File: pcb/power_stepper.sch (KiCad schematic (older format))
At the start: 48 parts, among them J2 Screw_Terminal, U16 UCC12040, U17 ISO7762, U2 powerSTEP01

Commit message: relayout
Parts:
- C1: footprint Capacitor_SMD:C_1206_3216Metric -> Capacitor_SMD:C_0805_2012Metric
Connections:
- net SENSEA_P: now reaches JP1.1 (A), RS1.2, RS2.2, RS3.2, RS7.2, U2.20 (SENSEA_S), U2.34 (SENSEA_P), U2.35 (SENSEA_P), U2.36 (SENSEA_P), U2.39 (SENSEA_P), U2.40 (SENSEA_P), U2.41 (SENSEA_P), U2.E10 (SENSEA_P), U2.E11 (SENSEA_P)
- net SENSEB_P: now reaches JP2.1 (A), RS4.2, RS5.2, RS6.2, RS8.2, U2.77 (SENSEB_P), U2.78 (SENSEB_P), U2.79 (SENSEB_P), U2.82 (SENSEB_P), U2.83 (SENSEB_P), U2.84 (SENSEB_P), U2.9 (SENSEB_S), U2.E12 (SENSEB_P), U2.E13 (SENSEB_P)
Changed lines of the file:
@@
 F 0 "C1" H 3618 7246 50  0000 L CNN
 F 1 "22uF" H 3618 7155 50  0000 L CNN
-F 2 "Capacitor_SMD:C_1206_3216Metric" H 3538 7050 50  0001 C CNN
+F 2 "Capacitor_SMD:C_0805_2012Metric" H 3538 7050 50  0001 C CNN
 F 3 "~" H 3500 7200 50  0001 C CNN
 	1    3500 7200
@@
 Text Label 3100 3050 2    50   ~ 0
 SM_SI
+Text Label 7550 4100 0    39   ~ 0
+SENSEB_P
+Text Label 7550 2850 0    39   ~ 0
+SENSEA_P
 $EndSCHEMATC

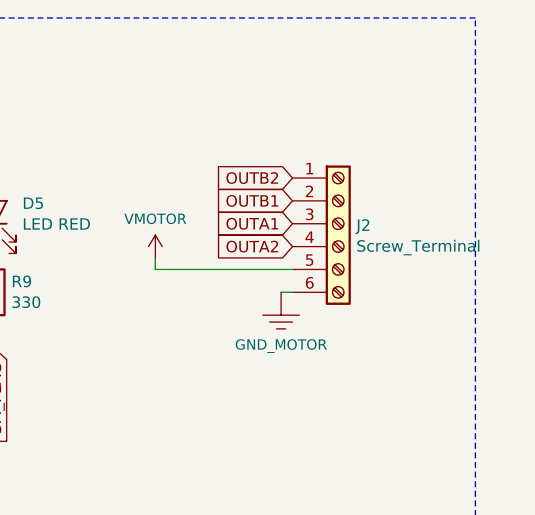
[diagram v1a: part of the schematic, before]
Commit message: stepper motor connector changed
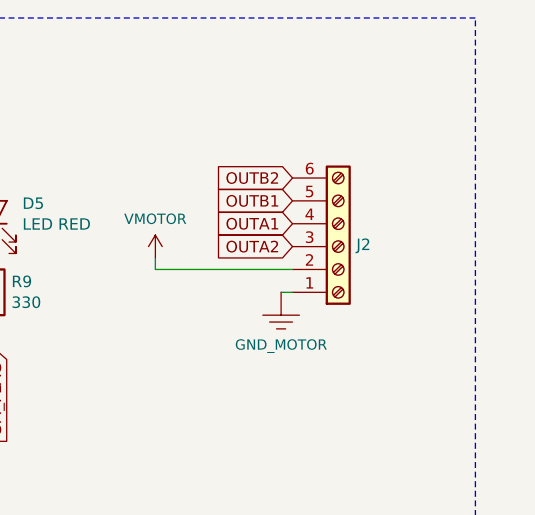
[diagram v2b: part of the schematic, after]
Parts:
- J2: value Screw_Terminal -> 1757284; footprint TerminalBlock_Phoenix:TerminalBlock_Phoenix_PT-1,5-6-5.0-H_1x06_P5.00mm_Horizontal -> Connector_Phoenix_MSTB:PhoenixContact_MSTBA_2,5_6-G-5,08_1x06_P5.08mm_Horizontal; DigiKey (none) -> 1757284
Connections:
- net GND_MOTOR: now also J2.1 (Pin_1); no longer J2.6 (Pin_6)
- net OUTA1: now also J2.4 (Pin_4); no longer J2.3 (Pin_3)
- net OUTA2: now also J2.3 (Pin_3); no longer J2.4 (Pin_4)
- net OUTB1: now also J2.5 (Pin_5); no longer J2.2 (Pin_2)
- net OUTB2: now also J2.6 (Pin_6); no longer J2.1 (Pin_1)
- net VMOTOR: now also J2.2 (Pin_2); no longer J2.5 (Pin_5)
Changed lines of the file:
@@
 EESchema Schematic File Version 4
+LIBS:keep_breathing_ctrl-cache
 EELAYER 30 0
 EELAYER END
@@
 L Connector:Screw_Terminal_01x06 J2
 U 1 1 5C39C166
-P 10500 1400
-F 0 "J2" H 10579 1392 50  0000 L CNN
-F 1 "Screw_Terminal" H 10579 1301 50  0000 L CNN
-F 2 "TerminalBlock_Phoenix:TerminalBlock_Phoenix_PT-1,5-6-5.0-H_1x06_P5.00mm_Horizontal" H 10500 1400 50  0001 C CNN
-F 3 "~" H 10500 1400 50  0001 C CNN
-	1    10500 1400
-	1    0    0    -1
-$EndComp
-$Comp
+P 10500 1500
+F 0 "J2" H 10579 1492 50  0000 L CNN
+F 1 "1757284" H 10579 1401 50  0001 L CNN
+F 2 "Connector_Phoenix_MSTB:PhoenixContact_MSTBA_2,5_6-G-5,08_1x06_P5.08mm_Horizontal" H 10500 1500 50  0001 C CNN
+F 3 "~" H 10500 1500 50  0001 C CNN
+F 4 "1757284" H 10500 1500 50  0001 C CNN "DigiKey"
+	1    10500 1500
+	1    0    0    1
+$EndComp
+$Comp

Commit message: routing isolators
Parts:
- D3, D5: footprint Diode_SMD:D_0805_2012Metric -> Diode_SMD:D_0603_1608Metric
- R11: footprint Resistor_SMD:R_0603_1608Metric -> Resistor_SMD:R_0402_1005Metric
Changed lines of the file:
@@
 F 0 "D5" V 9038 1232 50  0000 R CNN
 F 1 "LED RED" V 8947 1232 50  0000 R CNN
-F 2 "Diode_SMD:D_0805_2012Metric" H 9000 1350 50  0001 C CNN
+F 2 "Diode_SMD:D_0603_1608Metric" H 9000 1350 50  0001 C CNN
 F 3 "~" H 9000 1350 50  0001 C CNN
 	1    9000 1350
@@
 Wire Wire Line
 	9000 1550 9000 1500
-$Comp
-L Device:R R11
-U 1 1 5BEF92F7
-P 8900 4800
-F 0 "R11" H 8970 4846 50  0000 L CNN
-F 1 "330" H 8970 4755 50  0000 L CNN
-F 2 "Resistor_SMD:R_0603_1608Metric" V 8830 4800 50  0001 C CNN
-F 3 "~" H 8900 4800 50  0001 C CNN
-	1    8900 4800
-	1    0    0    -1
-$EndComp
-$Comp
-L Device:LED D3
-U 1 1 5BEF93CE
-P 8900 4450
-F 0 "D3" V 8938 4333 50  0000 R CNN
-F 1 "LED GRN" V 8847 4333 50  0000 R CNN
-F 2 "Diode_SMD:D_0805_2012Metric" H 8900 4450 50  0001 C CNN
-F 3 "~" H 8900 4450 50  0001 C CNN
-	1    8900 4450
-	0    -1   -1   0
-$EndComp
-Wire Wire Line
-	8900 4600 8900 4650
-Wire Wire Line
-	8900 4300 8900 4200
-Wire Wire Line
-	8900 4950 8900 5050
 Wire Wire Line
 	6650 2950 6650 2850
@@
 Wire Wire Line
 	3150 7000 3500 7000
-$Comp
-L ventilator-PowerSymbols:3V3_M #SUPPLY0106
-U 1 1 5EB9B2A5
-P 8900 4200
-F 0 "#SUPPLY0106" H 8950 4200 45  0001 L BNN
-F 1 "3V3_M" H 8900 4370 45  0000 C CNN
-F 2 "" H 8900 4200 50  0001 C CNN
-F 3 "" H 8900 4200 60  0001 C CNN
-	1    8900 4200
-	1    0    0    -1
-$EndComp
 $Comp
 L ventilator-PowerSymbols:3V3_M #SUPPLY0107
@@
 $EndComp
 $Comp
+L ventilator-PowerSymbols:GND_MOTOR #GND0109
+U 1 1 5EB3C9E7
+P 10150 5200
+F 0 "#GND0109" H 10200 5150 45  0001 L BNN
+F 1 "GND_MOTOR" H 10150 4970 45  0000 C CNN
+F 2 "" H 10150 5200 50  0001 C CNN
+F 3 "" H 10150 5100 60  0001 C CNN
+	1    10150 5200
+	1    0    0    -1
+$EndComp
+$Comp
+L ventilator-PowerSymbols:GND_MOTOR #GND0110
+U 1 1 5EB42E98
+P 4150 7450
+F 0 "#GND0110" H 4200 7400 45  0001 L BNN
+F 1 "GND_MOTOR" H 4150 7220 45  0000 C CNN
+F 2 "" H 4150 7450 50  0001 C CNN
+F 3 "" H 4150 7350 60  0001 C CNN
+	1    4150 7450
+	1    0    0    -1
+$EndComp
+$Comp
+L ventilator-PowerSymbols:GND_MOTOR #GND0111
+U 1 1 5EB70716
+P 3650 6600
+F 0 "#GND0111" H 3700 6550 45  0001 L BNN
+F 1 "GND_MOTOR" H 3650 6370 45  0000 C CNN
+F 2 "" H 3650 6600 50  0001 C CNN
+F 3 "" H 3650 6500 60  0001 C CNN
+	1    3650 6600
+	1    0    0    -1
+$EndComp
+$Comp
+L ventilator-PowerSymbols:GND_MOTOR #GND0112
+U 1 1 5EB70F8C
+P 2800 4000
+F 0 "#GND0112" H 2850 3950 45  0001 L BNN
+F 1 "GND_MOTOR" H 2800 3770 45  0000 C CNN
+F 2 "" H 2800 4000 50  0001 C CNN
+F 3 "" H 2800 3900 60  0001 C CNN
+	1    2800 4000
+	1    0    0    -1
+$EndComp
+$Comp
+L ventilator-PowerSymbols:GND_MOTOR #GND0114
+U 1 1 5EB73041
+P 3550 2900
+F 0 "#GND0114" H 3600 2850 45  0001 L BNN
+F 1 "GND_MOTOR" H 3550 2670 45  0000 C CNN
+F 2 "" H 3550 2900 50  0001 C CNN
+F 3 "" H 3550 2800 60  0001 C CNN
+	1    3550 2900
+	1    0    0    -1
+$EndComp
+$Comp
+L ventilator-PowerSymbols:GND_MOTOR #GND0115
+U 1 1 5EBD4224
+P 6500 6950
+F 0 "#GND0115" H 6550 6900 45  0001 L BNN
+F 1 "GND_MOTOR" H 6500 6720 45  0000 C CNN
+F 2 "" H 6500 6950 50  0001 C CNN
+F 3 "" H 6500 6850 60  0001 C CNN
+	1    6500 6950
+	1    0    0    -1
+$EndComp
+Wire Wire Line
+	2700 3200 3100 3200
+Wire Wire Line
+	2700 3050 3100 3050
+Text Label 3100 3050 2    50   ~ 0
+SM_SI
+Text Label 7550 4100 0    39   ~ 0
+SENSEB_P
+Text Label 7550 2850 0    39   ~ 0
+SENSEA_P
+$Comp
 L ventilator-PowerSymbols:GND_MOTOR #GND0108
 U 1 1 5EAD8892
@@
 $EndComp
 $Comp
-L ventilator-PowerSymbols:GND_MOTOR #GND0109
-U 1 1 5EB3C9E7
-P 10150 5200
-F 0 "#GND0109" H 10200 5150 45  0001 L BNN
-F 1 "GND_MOTOR" H 10150 4970 45  0000 C CNN
-F 2 "" H 10150 5200 50  0001 C CNN
-F 3 "" H 10150 5100 60  0001 C CNN
-	1    10150 5200
-	1    0    0    -1
-$EndComp
-$Comp
-L ventilator-PowerSymbols:GND_MOTOR #GND0110
-U 1 1 5EB42E98
-P 4150 7450
-F 0 "#GND0110" H 4200 7400 45  0001 L BNN
-F 1 "GND_MOTOR" H 4150 7220 45  0000 C CNN
-F 2 "" H 4150 7450 50  0001 C CNN
-F 3 "" H 4150 7350 60  0001 C CNN
-	1    4150 7450
-	1    0    0    -1
-$EndComp
-$Comp
-L ventilator-PowerSymbols:GND_MOTOR #GND0111
-U 1 1 5EB70716
-P 3650 6600
-F 0 "#GND0111" H 3700 6550 45  0001 L BNN
-F 1 "GND_MOTOR" H 3650 6370 45  0000 C CNN
-F 2 "" H 3650 6600 50  0001 C CNN
-F 3 "" H 3650 6500 60  0001 C CNN
-	1    3650 6600
-	1    0    0    -1
-$EndComp
-$Comp
-L ventilator-PowerSymbols:GND_MOTOR #GND0112
-U 1 1 5EB70F8C
-P 2800 4000
-F 0 "#GND0112" H 2850 3950 45  0001 L BNN
-F 1 "GND_MOTOR" H 2800 3770 45  0000 C CNN
-F 2 "" H 2800 4000 50  0001 C CNN
-F 3 "" H 2800 3900 60  0001 C CNN
-	1    2800 4000
-	1    0    0    -1
-$EndComp
-$Comp
-L ventilator-PowerSymbols:GND_MOTOR #GND0114
-U 1 1 5EB73041
-P 3550 2900
-F 0 "#GND0114" H 3600 2850 45  0001 L BNN
-F 1 "GND_MOTOR" H 3550 2670 45  0000 C CNN
-F 2 "" H 3550 2900 50  0001 C CNN
-F 3 "" H 3550 2800 60  0001 C CNN
-	1    3550 2900
-	1    0    0    -1
-$EndComp
-$Comp
-L ventilator-PowerSymbols:GND_MOTOR #GND0115
-U 1 1 5EBD4224
-P 6500 6950
-F 0 "#GND0115" H 6550 6900 45  0001 L BNN
-F 1 "GND_MOTOR" H 6500 6720 45  0000 C CNN
-F 2 "" H 6500 6950 50  0001 C CNN
-F 3 "" H 6500 6850 60  0001 C CNN
-	1    6500 6950
-	1    0    0    -1
-$EndComp
-Wire Wire Line
-	2700 3200 3100 3200
-Wire Wire Line
-	2700 3050 3100 3050
-Text Label 3100 3050 2    50   ~ 0
-SM_SI
-Text Label 7550 4100 0    39   ~ 0
-SENSEB_P
-Text Label 7550 2850 0    39   ~ 0
-SENSEA_P
+L ventilator-PowerSymbols:3V3_M #SUPPLY0106
+U 1 1 5EB9B2A5
+P 8900 4200
+F 0 "#SUPPLY0106" H 8950 4200 45  0001 L BNN
+F 1 "3V3_M" H 8900 4370 45  0000 C CNN
+F 2 "" H 8900 4200 50  0001 C CNN
+F 3 "" H 8900 4200 60  0001 C CNN
+	1    8900 4200
+	1    0    0    -1
+$EndComp
+Wire Wire Line
+	8900 4950 8900 5050
+Wire Wire Line
+	8900 4300 8900 4200
+Wire Wire Line
+	8900 4600 8900 4650
+$Comp
+L Device:LED D3
+U 1 1 5BEF93CE
+P 8900 4450
+F 0 "D3" V 8938 4333 50  0000 R CNN
+F 1 "LED GRN" V 8847 4333 50  0000 R CNN
+F 2 "Diode_SMD:D_0603_1608Metric" H 8900 4450 50  0001 C CNN
+F 3 "~" H 8900 4450 50  0001 C CNN
+	1    8900 4450
+	0    -1   -1   0
+$EndComp
+$Comp
+L Device:R R11
+U 1 1 5BEF92F7
+P 8900 4800
+F 0 "R11" H 8970 4846 50  0000 L CNN
+F 1 "330" H 8970 4755 50  0000 L CNN
+F 2 "Resistor_SMD:R_0402_1005Metric" V 8830 4800 50  0001 C CNN
+F 3 "~" H 8900 4800 50  0001 C CNN
+	1    8900 4800
+	1    0    0    -1
+$EndComp
 $EndSCHEMATC

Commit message: updating planes
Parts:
- added C74: 0.1uF, Capacitor_SMD:C_0402_1005Metric, symbol Device:C_Small
- R39: value SEL -> 100k
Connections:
- net GND: now also U16.4 (SYNC), C74.2
- net +5V: now reaches C33.1, C34.1, U16.1 (EN), U16.3 (VINP)
- net +3V3: now reaches U17.1 (VCC1)
- net +3V3: now also C74.1
- no-connect marks 3 -> 4
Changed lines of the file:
@@
 U 1 1 5E9880D0
 P 2100 1550
+AR Path="/5E9880D0" Ref="U16"  Part="1"
+AR Path="/5E968E64/5E9880D0" Ref="U16"  Part="1"
 F 0 "U16" H 1650 2250 50  0000 L CNB
 F 1 "UCC12040" H 1650 2150 50  0000 L CNN
@@
 P 2750 1350
 F 0 "R39" H 2750 1550 50  0000 L CNN
-F 1 "SEL" H 2750 1200 50  0000 L CNN
+F 1 "100k" H 2750 1200 50  0000 L CNN
 F 2 "Resistor_SMD:R_0402_1005Metric" H 2750 1350 50  0001 C CNN
 F 3 "~" H 2750 1350 50  0001 C CNN
@@
 	1    0    0    -1
 $EndComp
+$Comp
+L power:+5V #PWR0141
+U 1 1 5EB2F2C1
+P 800 1050
+F 0 "#PWR0141" H 800 900 50  0001 C CNN
+F 1 "+5V" H 815 1223 50  0000 C CNN
+F 2 "" H 800 1050 50  0001 C CNN
+F 3 "" H 800 1050 50  0001 C CNN
+	1    800  1050
+	1    0    0    -1
+$EndComp
+NoConn ~ 1550 1600
+$Comp
+L power:GND #PWR0142
+U 1 1 5EB83B21
+P 1450 1525
+F 0 "#PWR0142" H 1450 1275 50  0001 C CNN
+F 1 "GND" H 1455 1352 50  0000 C CNN
+F 2 "" H 1450 1525 50  0001 C CNN
+F 3 "" H 1450 1525 50  0001 C CNN
+	1    1450 1525
+	1    0    0    -1
+$EndComp
+Wire Wire Line
+	1550 1500 1450 1500
+Wire Wire Line
+	1450 1500 1450 1525
+$Comp
+L power:+3V3 #PWR0144
+U 1 1 5EC0803D
+P 1400 2700
+F 0 "#PWR0144" H 1400 2550 50  0001 C CNN
+F 1 "+3V3" H 1415 2873 50  0000 C CNN
+F 2 "" H 1400 2700 50  0001 C CNN
+F 3 "" H 1400 2700 50  0001 C CNN
+	1    1400 2700
+	1    0    0    -1
+$EndComp
+Wire Wire Line
+	1500 2700 1400 2700
+$Comp
+L Device:C_Small C74
+U 1 1 5EC35AA7
+P 1175 4800
+F 0 "C74" H 1225 4900 50  0000 L CNN
+F 1 "0.1uF" H 1225 4700 50  0000 L CNN
+F 2 "Capacitor_SMD:C_0402_1005Metric" H 1213 4650 50  0001 C CNN
+F 3 "~" H 1175 4800 50  0001 C CNN
+	1    1175 4800
+	1    0    0    -1
+$EndComp
+$Comp
+L power:GND #PWR0145
+U 1 1 5EC6EB33
+P 1175 4950
+F 0 "#PWR0145" H 1175 4700 50  0001 C CNN
+F 1 "GND" H 1180 4777 50  0000 C CNN
+F 2 "" H 1175 4950 50  0001 C CNN
+F 3 "" H 1175 4950 50  0001 C CNN
+	1    1175 4950
+	1    0    0    -1
+$EndComp
+$Comp
+L power:+3V3 #PWR0228
+U 1 1 5EC9B6D5
+P 1175 4625
+F 0 "#PWR0228" H 1175 4475 50  0001 C CNN
+F 1 "+3V3" H 1190 4798 50  0000 C CNN
+F 2 "" H 1175 4625 50  0001 C CNN
+F 3 "" H 1175 4625 50  0001 C CNN
+	1    1175 4625
+	1    0    0    -1
+$EndComp
+Wire Wire Line
+	1175 4625 1175 4700
+Wire Wire Line
+	1175 4900 1175 4950
 $EndSCHEMATC

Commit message: fixing missed footprints
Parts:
- U2: footprint Klofas-Motor:powerSTEP01 -> SMD:powerSTEP01
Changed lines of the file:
@@
 F 0 "U2" H 5750 11165 50  0000 C CNN
 F 1 "powerSTEP01" H 5750 11074 50  0000 C CNN
-F 2 "Klofas-Motor:powerSTEP01" H 5700 4800 50  0001 C CNN
+F 2 "SMD:powerSTEP01" H 5700 4800 50  0001 C CNN
 F 3 "" H 5700 4800 50  0001 C CNN
 	1    5700 5900
